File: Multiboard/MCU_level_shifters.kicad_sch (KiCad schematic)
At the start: 64 parts, among them Q1 Q_NMOS, Q10 Q_NMOS, Q11 Q_NMOS, Q12 Q_NMOS, Q13 Q_NMOS, Q14 Q_NMOS, Q15 Q_NMOS, Q16 Q_NMOS, Q17 Q_NMOS, Q18 Q_NMOS, Q2 Q_NMOS, Q3 Q_NMOS, Q4 Q_NMOS, Q5 Q_NMOS, Q6 Q_NMOS, Q7 Q_NMOS, Q8 Q_NMOS, Q9 Q_NMOS, SW3 SW_SPST, SW4 SW_SPST, SW5 SW_SPST, SW6 SW_SPST, SW7 SW_SPST, U4 USART1, U5 I2C1, U6 SPI1, U7 ADC, U8 GPIO-PWM

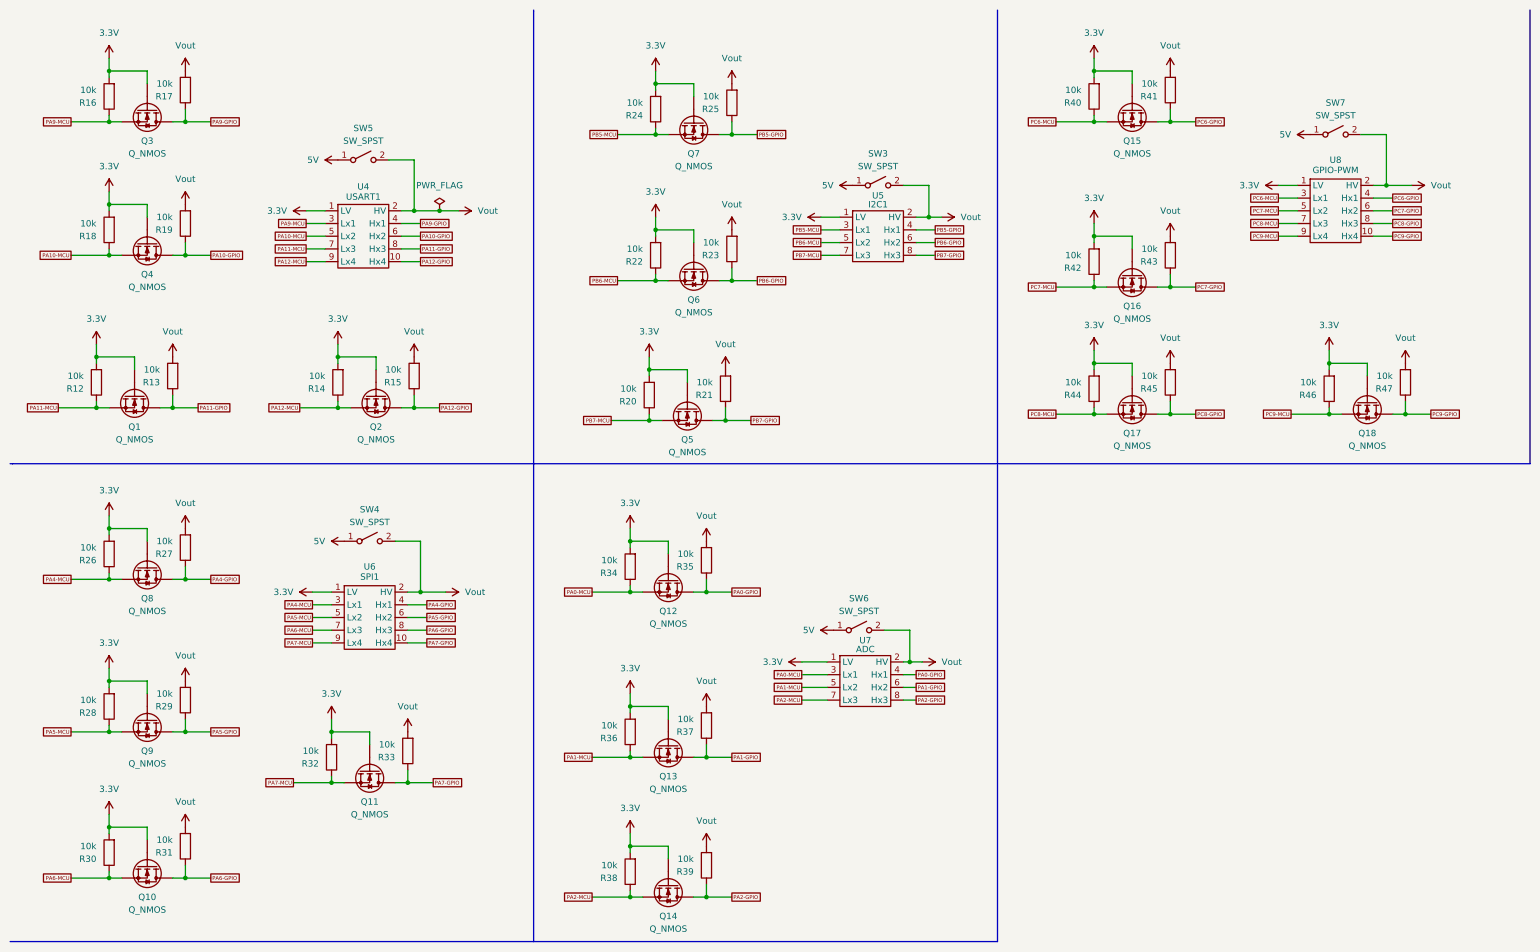
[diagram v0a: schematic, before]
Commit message: FIxed level shifter implementation
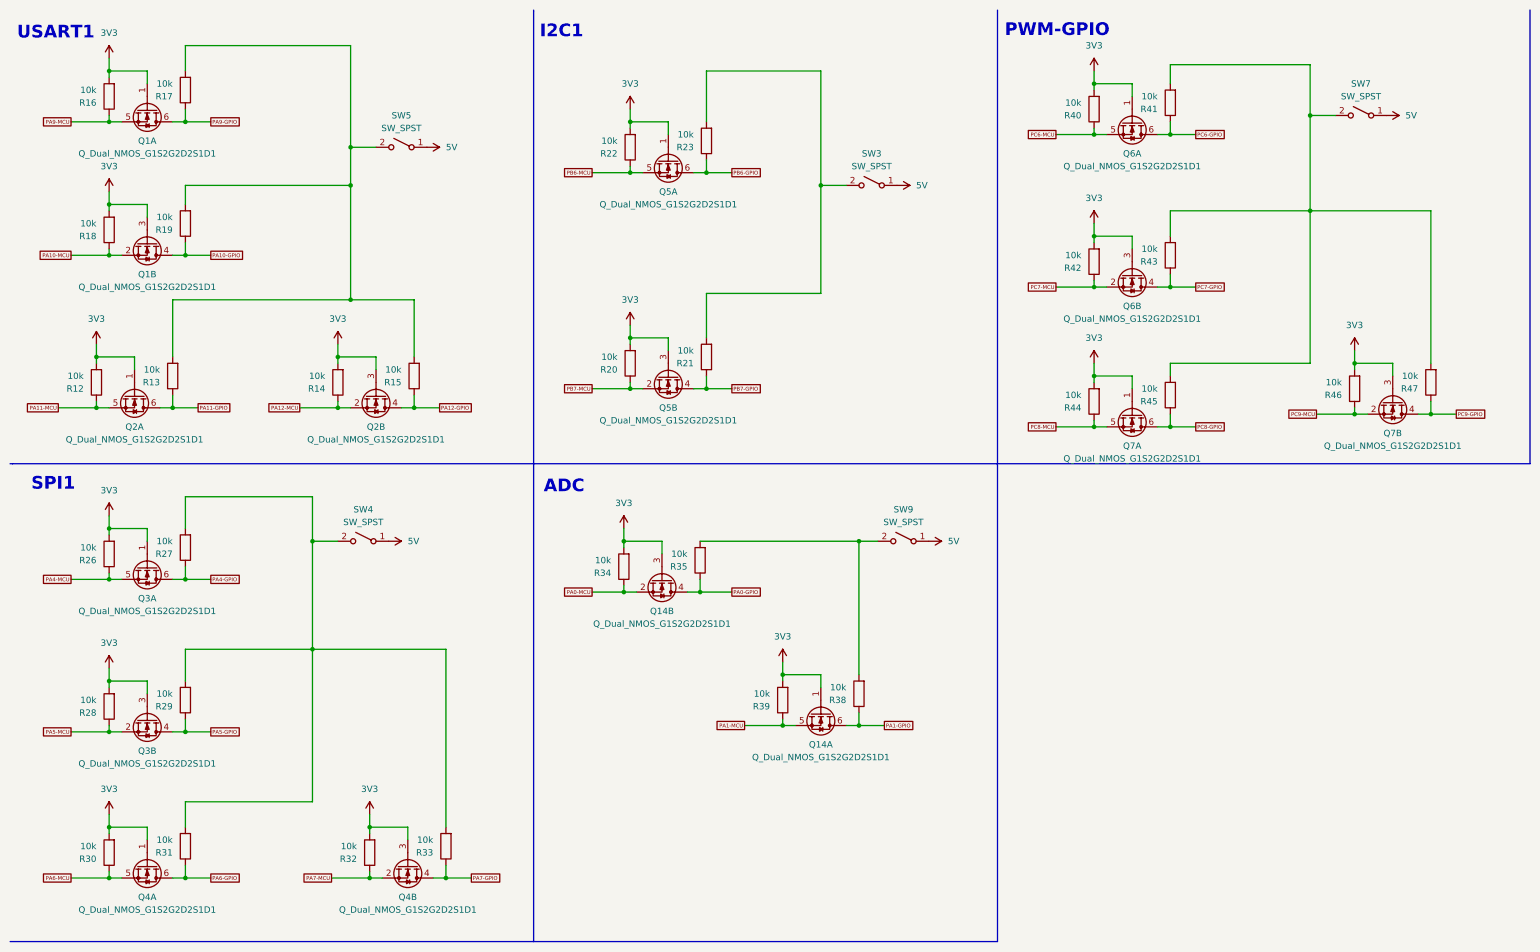
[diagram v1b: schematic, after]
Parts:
- removed Q1, Q10, Q11, Q15, Q16, Q17, Q18, Q2, Q3, Q4, Q5, Q6, Q7, Q8, Q9: Q_NMOS, Package_TO_SOT_SMD:SOT-23, symbol Device:Q_NMOS
- removed Q12, Q13, Q14: Q_NMOS, Package_TO_SOT_SMD:SOT-23-3, symbol Device:Q_NMOS
- removed R24, R25, R36, R37: 10k, Resistor_SMD:R_0603_1608Metric_Pad0.98x0.95mm_HandSolder, symbol Device:R
- removed SW6: SW_SPST, Button_Switch_THT:SW_DIP_SPSTx01_Slide_9.78x4.72mm_W7.62mm_P2.54mm, symbol Switch:SW_SPST
- removed U4: USART1, Level_Shifter:Level_Shifter_3_CH, symbol Level_Shifter:Level_Shifter_4_BD
- removed U5: I2C1, Level_Shifter:Level_Shifter_3_CH, symbol Level_Shifter:Level_Shifter_3_BD
- removed U6: SPI1, Level_Shifter:Level_Shifter_3_CH, symbol Level_Shifter:Level_Shifter_4_BD
- removed U7: ADC, Level_Shifter:Level_Shifter_3_CH, symbol Level_Shifter:Level_Shifter_3_BD
- removed U8: GPIO-PWM, Level_Shifter:Level_Shifter_3_CH, symbol Level_Shifter:Level_Shifter_4_BD
- added Q1, Q14, Q2, Q3, Q4, Q5, Q6, Q7: Q_Dual_NMOS_G1S2G2D2S1D1, Package_SO:SOIC-8_3.9x4.9mm_P1.27mm, symbol Transistor_FET:Q_Dual_NMOS_G1S2G2D2S1D1
- added SW9: SW_SPST, Button_Switch_THT:SW_DIP_SPSTx01_Slide_9.78x4.72mm_W7.62mm_P2.54mm, symbol Switch:SW_SPST
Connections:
- net PA2-GPIO is gone; now on net PA1-MCU: R39.1
- net PA2-MCU is gone; now on net PA1-GPIO: R38.1
- net 5V: now also SW9.1 (A)
- net PA0-GPIO: now also Q14.4 (D)
- net PA0-MCU: now also Q14.2 (S)
- net PA1-GPIO: now also Q14.6 (D)
- net PA1-MCU: now also Q14.5 (S)
- net PA10-GPIO: now also Q1.4 (D)
- net PA10-MCU: now also Q1.2 (S)
- net PA11-GPIO: now also Q2.6 (D)
- net PA11-MCU: now also Q2.5 (S)
- net PA12-GPIO: now also Q2.4 (D)
- net PA12-MCU: now also Q2.2 (S)
- net PA4-GPIO: now also Q3.6 (D)
- net PA4-MCU: now also Q3.5 (S)
- net PA5-GPIO: now also Q3.4 (D)
- net PA5-MCU: now also Q3.2 (S)
- net PA6-GPIO: now also Q4.6 (D)
- net PA6-MCU: now also Q4.5 (S)
- net PA7-GPIO: now also Q4.4 (D)
- net PA7-MCU: now also Q4.2 (S)
- net PA9-GPIO: now also Q1.6 (D)
- net PA9-MCU: now also Q1.5 (S)
- net PB6-GPIO: now also Q5.6 (D)
- net PB6-MCU: now also Q5.5 (S)
- net PB7-GPIO: now also Q5.4 (D)
- net PB7-MCU: now also Q5.2 (S)
- net PC6-GPIO: now also Q6.6 (D)
- net PC6-MCU: now also Q6.5 (S)
- net PC7-GPIO: now also Q6.4 (D)
- net PC7-MCU: now also Q6.2 (S)
- net PC8-GPIO: now also Q7.6 (D)
- net PC8-MCU: now also Q7.5 (S)
- net PC9-GPIO: now also Q7.4 (D)
- net PC9-MCU: now also Q7.2 (S)
- net 3.3V renamed 3V3
- net 3V3: now also R39.2, Q1.1 (G), Q1.3 (G), Q14.1 (G), Q14.3 (G), Q2.1 (G), Q2.3 (G), Q3.1 (G), Q3.3 (G), Q4.1 (G), Q4.3 (G), Q5.1 (G), Q5.3 (G), Q6.1 (G), Q6.3 (G), Q7.1 (G), Q7.3 (G); no longer R38.2
- removed net Vout: R13.2, R15.2, R17.2, R19.2, R21.2, R23.2, R27.2, R29.2, R31.2, R33.2, R35.2, R39.2, R41.2, R43.2, R45.2, R47.2, SW3.2 (B), SW4.2 (B), SW5.2 (B), SW7.2 (B)
- new net: R41.2, R43.2, R45.2, R47.2, SW7.2 (B)
- new net: R21.2, R23.2, SW3.2 (B)
- new net: R13.2, R15.2, R17.2, R19.2, SW5.2 (B)
- new net: R27.2, R29.2, R31.2, R33.2, SW4.2 (B)
- new net: R35.2, R38.2, SW9.2 (B)
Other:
- note added: "ADC"
- note added: "I2C1"
- note added: "PWM-GPIO"
- note added: "SPI1"
- note added: "USART1"
- moved on the sheet: R20, R21, R22, R23, R32, R33, R34, R35, R40, R41, R44, R45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

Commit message: Fixed bus implementation
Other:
- moved on the sheet: Q2A
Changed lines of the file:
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@@
 	(text "SPI1"
 		(exclude_from_sim no)
-		(at 20.574 106.68 0)
+		(at 18.796 106.934 0)
 		(effects
 			(font
@@
 	(symbol
 		(lib_id "Transistor_FET:Q_Dual_NMOS_G1S2G2D2S1D1")
-		(at 85.09 88.9 270)
-		(unit 2)
+		(at 36.83 88.9 270)
+		(unit 1)
 		(exclude_from_sim no)
 		(in_bom yes)
@@
 		(fields_autoplaced yes)
 		(property "Reference" "Q2"
-			(at 85.09 95.25 90)
+			(at 36.83 95.25 90)
 			(effects
 				(font
@@
 		)
 		(property "Value" "Q_Dual_NMOS_G1S2G2D2S1D1"
-			(at 85.09 97.79 90)
+			(at 36.83 97.79 90)
 			(effects
 				(font
@@
 		)
 		(property "Footprint" "Package_SO:SOIC-8_3.9x4.9mm_P1.27mm"
-			(at 85.09 93.98 0)
+			(at 36.83 93.98 0)
 			(effects
 				(font
@@
 		)
 		(property "Datasheet" "~"
-			(at 85.09 93.98 0)
+			(at 36.83 93.98 0)
 			(effects
 				(font
@@
 		)
 		(property "Description" "Dual NMOS transistor, 6 pin package"
-			(at 85.09 88.9 0)
+			(at 36.83 88.9 0)
 			(effects
 				(font
@@
 				(path "/9ed4a389-3aa7-41f1-b239-280eb7f09ef1/47d00c33-b241-4dd6-bf0c-4e5c6f2dc35e"
 					(reference "Q2")
-					(unit 2)
+					(unit 1)
 				)
 			)
@@
 	(symbol
 		(lib_id "Transistor_FET:Q_Dual_NMOS_G1S2G2D2S1D1")
-		(at 36.83 88.9 270)
-		(unit 1)
+		(at 85.09 88.9 270)
+		(unit 2)
 		(exclude_from_sim no)
 		(in_bom yes)
@@
 		(fields_autoplaced yes)
 		(property "Reference" "Q2"
-			(at 36.83 95.25 90)
+			(at 85.09 95.25 90)
 			(effects
 				(font
@@
 		)
 		(property "Value" "Q_Dual_NMOS_G1S2G2D2S1D1"
-			(at 36.83 97.79 90)
+			(at 85.09 97.79 90)
 			(effects
 				(font
@@
 		)
 		(property "Footprint" "Package_SO:SOIC-8_3.9x4.9mm_P1.27mm"
-			(at 36.83 93.98 0)
+			(at 85.09 93.98 0)
 			(effects
 				(font
@@
 		)
 		(property "Datasheet" "~"
-			(at 36.83 93.98 0)
+			(at 85.09 93.98 0)
 			(effects
 				(font
@@
 		)
 		(property "Description" "Dual NMOS transistor, 6 pin package"
-			(at 36.83 88.9 0)
+			(at 85.09 88.9 0)
 			(effects
 				(font
@@
 				(path "/9ed4a389-3aa7-41f1-b239-280eb7f09ef1/47d00c33-b241-4dd6-bf0c-4e5c6f2dc35e"
 					(reference "Q2")
-					(unit 1)
+					(unit 2)
 				)
 			)

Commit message: changed mosfet footprint
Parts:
- added unit 2 of Q1
- added unit 1 of Q14
- added unit 2 of Q2
- added unit 1 of Q3
- added unit 1 of Q4
- added unit 1 of Q5
- added unit 1 of Q6
- added unit 1 of Q7
- Q1, Q14, Q2, Q3, Q4, Q5, Q6, Q7: footprint Package_SO:SOIC-8_3.9x4.9mm_P1.27mm -> Package_TO_SOT_SMD:SOT-23-6_Handsoldering
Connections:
- net 3V3: now also Q1.3 (G), Q14.1 (G), Q2.3 (G), Q3.1 (G), Q4.1 (G), Q5.1 (G), Q6.1 (G), Q7.1 (G); no longer Q1.3 (G), Q14.1 (G), Q2.3 (G), Q3.1 (G), Q4.1 (G), Q5.1 (G), Q6.1 (G), Q7.1 (G)
- net PA1-GPIO: now also Q14.6 (D); no longer Q14.6 (D)
- net PA1-MCU: now also Q14.5 (S); no longer Q14.5 (S)
- net PA10-GPIO: now also Q1.4 (D); no longer Q1.4 (D)
- net PA10-MCU: now also Q1.2 (S); no longer Q1.2 (S)
- net PA12-GPIO: now also Q2.4 (D); no longer Q2.4 (D)
- net PA12-MCU: now also Q2.2 (S); no longer Q2.2 (S)
- net PA4-GPIO: now also Q3.6 (D); no longer Q3.6 (D)
- net PA4-MCU: now also Q3.5 (S); no longer Q3.5 (S)
- net PA6-GPIO: now also Q4.6 (D); no longer Q4.6 (D)
- net PA6-MCU: now also Q4.5 (S); no longer Q4.5 (S)
- net PB6-GPIO: now also Q5.6 (D); no longer Q5.6 (D)
- net PB6-MCU: now also Q5.5 (S); no longer Q5.5 (S)
- net PC6-GPIO: now also Q6.6 (D); no longer Q6.6 (D)
- net PC6-MCU: now also Q6.5 (S); no longer Q6.5 (S)
- net PC8-GPIO: now also Q7.6 (D); no longer Q7.6 (D)
- net PC8-MCU: now also Q7.5 (S); no longer Q7.5 (S)
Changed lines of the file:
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@@
 			)
 		)
-		(property "Footprint" "Package_SO:SOIC-8_3.9x4.9mm_P1.27mm"
+		(property "Footprint" "Package_TO_SOT_SMD:SOT-23-6_Handsoldering"
 			(at 91.44 187.96 0)
 			(effects
@@
 			)
 		)
-		(property "Footprint" "Package_SO:SOIC-8_3.9x4.9mm_P1.27mm"
+		(property "Footprint" "Package_TO_SOT_SMD:SOT-23-6_Handsoldering"
 			(at 39.37 187.96 0)
 			(effects
@@
 			)
 		)
-		(property "Footprint" "Package_SO:SOIC-8_3.9x4.9mm_P1.27mm"
+		(property "Footprint" "Package_TO_SOT_SMD:SOT-23-6_Handsoldering"
 			(at 143.51 90.17 0)
 			(effects
@@
 			)
 		)
-		(property "Footprint" "Package_SO:SOIC-8_3.9x4.9mm_P1.27mm"
+		(property "Footprint" "Package_TO_SOT_SMD:SOT-23-6_Handsoldering"
 			(at 143.51 46.99 0)
 			(effects
@@
 			)
 		)
-		(property "Footprint" "Package_SO:SOIC-8_3.9x4.9mm_P1.27mm"
+		(property "Footprint" "Package_TO_SOT_SMD:SOT-23-6_Handsoldering"
 			(at 39.37 36.83 0)
 			(effects
@@
 			)
 		)
-		(property "Footprint" "Package_SO:SOIC-8_3.9x4.9mm_P1.27mm"
+		(property "Footprint" "Package_TO_SOT_SMD:SOT-23-6_Handsoldering"
 			(at 39.37 63.5 0)
 			(effects
@@
 			)
 		)
-		(property "Footprint" "Package_SO:SOIC-8_3.9x4.9mm_P1.27mm"
+		(property "Footprint" "Package_TO_SOT_SMD:SOT-23-6_Handsoldering"
 			(at 36.83 93.98 0)
 			(effects
@@
 			)
 		)
-		(property "Footprint" "Package_SO:SOIC-8_3.9x4.9mm_P1.27mm"
+		(property "Footprint" "Package_TO_SOT_SMD:SOT-23-6_Handsoldering"
 			(at 85.09 93.98 0)
 			(effects
@@
 			)
 		)
-		(property "Footprint" "Package_SO:SOIC-8_3.9x4.9mm_P1.27mm"
+		(property "Footprint" "Package_TO_SOT_SMD:SOT-23-6_Handsoldering"
 			(at 39.37 158.75 0)
 			(effects
@@
 			)
 		)
-		(property "Footprint" "Package_SO:SOIC-8_3.9x4.9mm_P1.27mm"
+		(property "Footprint" "Package_TO_SOT_SMD:SOT-23-6_Handsoldering"
 			(at 39.37 128.27 0)
 			(effects
@@
 			)
 		)
-		(property "Footprint" "Package_SO:SOIC-8_3.9x4.9mm_P1.27mm"
+		(property "Footprint" "Package_TO_SOT_SMD:SOT-23-6_Handsoldering"
 			(at 236.22 69.85 0)
 			(effects
@@
 			)
 		)
-		(property "Footprint" "Package_SO:SOIC-8_3.9x4.9mm_P1.27mm"
+		(property "Footprint" "Package_TO_SOT_SMD:SOT-23-6_Handsoldering"
 			(at 236.22 39.37 0)
 			(effects
@@
 			)
 		)
-		(property "Footprint" "Package_SO:SOIC-8_3.9x4.9mm_P1.27mm"
+		(property "Footprint" "Package_TO_SOT_SMD:SOT-23-6_Handsoldering"
 			(at 288.29 95.25 0)
 			(effects
@@
 			)
 		)
-		(property "Footprint" "Package_SO:SOIC-8_3.9x4.9mm_P1.27mm"
+		(property "Footprint" "Package_TO_SOT_SMD:SOT-23-6_Handsoldering"
 			(at 236.22 97.79 0)
 			(effects
@@
 			)
 		)
-		(property "Footprint" "Package_SO:SOIC-8_3.9x4.9mm_P1.27mm"
+		(property "Footprint" "Package_TO_SOT_SMD:SOT-23-6_Handsoldering"
 			(at 142.24 130.81 0)
 			(effects
@@
 			)
 		)
-		(property "Footprint" "Package_SO:SOIC-8_3.9x4.9mm_P1.27mm"
+		(property "Footprint" "Package_TO_SOT_SMD:SOT-23-6_Handsoldering"
 			(at 173.99 157.48 0)
 			(effects

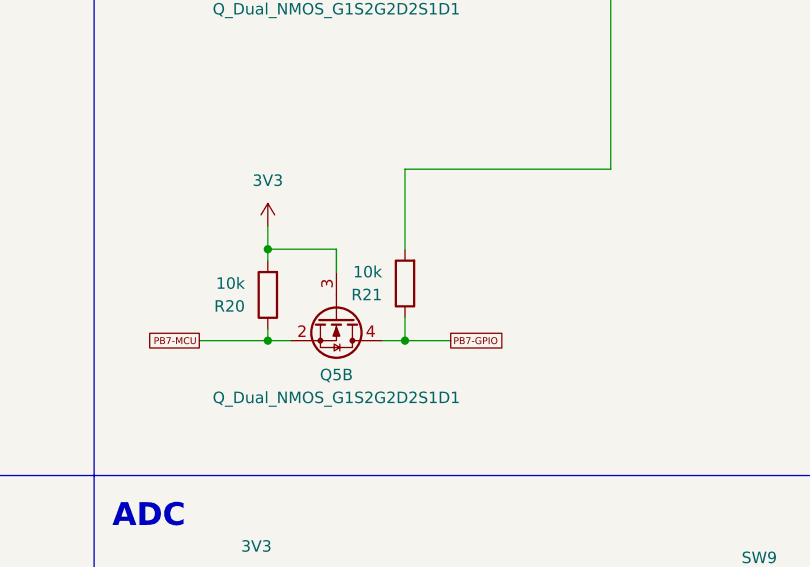
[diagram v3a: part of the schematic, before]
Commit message: positioned USART1 and I2C1 level shifters
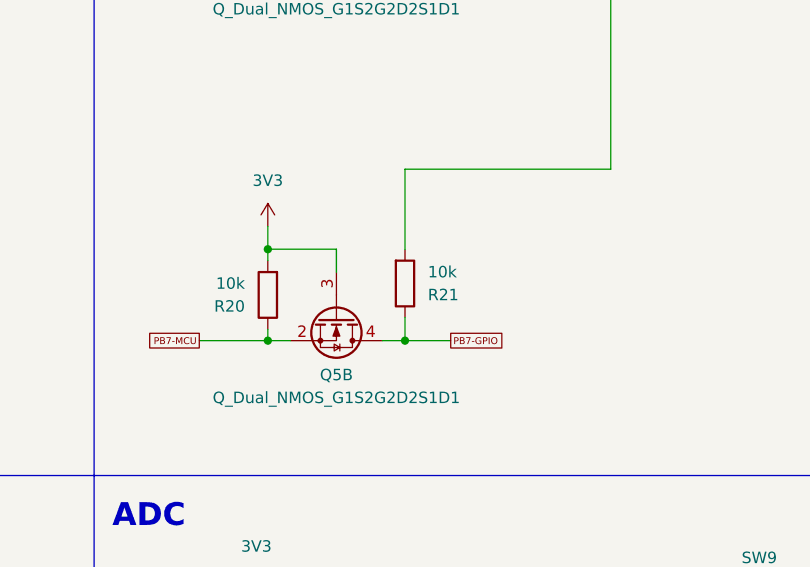
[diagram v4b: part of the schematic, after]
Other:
- moved on the sheet: R21
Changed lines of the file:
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@@
 	(symbol
 		(lib_id "Device:R")
-		(at 151.13 81.28 180)
+		(at 151.13 81.28 0)
+		(mirror x)
 		(unit 1)
 		(exclude_from_sim no)
@@
 		(on_board yes)
 		(dnp no)
-		(fields_autoplaced yes)
 		(property "Reference" "R21"
-			(at 148.59 82.5501 0)
+			(at 153.67 82.5501 0)
 			(effects
 				(font
@@
 		)
 		(property "Value" "10k"
-			(at 148.59 80.0101 0)
+			(at 153.67 80.0101 0)
 			(effects
 				(font
@@
 		)
 		(property "Footprint" "Resistor_SMD:R_0603_1608Metric_Pad0.98x0.95mm_HandSolder"
-			(at 152.908 81.28 90)
+			(at 149.352 81.28 90)
 			(effects
 				(font
